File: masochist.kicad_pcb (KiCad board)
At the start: 2 copper layers, 77 parts, among them J1 USB_C_Receptacle_USB2.0, J2 AVR-ISP-6, SW1 RESET, SW2 SW_Push, U1 ATmega328P-PU, Y1 Crystal

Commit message: Project is NOT dead, components are roughly in place
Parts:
- moved Y1 225.3 mm to (232.3, 48.8)
- moved R5 222.6 mm to (201.9, 46.2)
- moved C1 222.1 mm to (227.3, 49.9), turned to 90 degrees
- moved C5 221.5 mm to (232.3, 34.2), turned to 180 degrees
- moved C2 211.0 mm to (242.1, 49.9), turned to 90 degrees
- moved R4 206.2 mm to (201.9, 43.4)
- moved R2 205.1 mm to (201.9, 40.6)
- moved R7 203.6 mm to (201.9, 51.8)
- moved R1 202.8 mm to (201.9, 35.1)
- moved R3 202.0 mm to (201.9, 37.8)
- moved R6 200.6 mm to (201.9, 49.0)
- moved DZ1 199.2 mm to (181.0, 51.8), turned to 180 degrees
- moved C4 198.4 mm to (220.0, 47.6)
- moved DZ2 197.3 mm to (181.0, 49.0), turned to 180 degrees
- moved SW2 162.2 mm to (129.2, 34.7)
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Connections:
- U1 pad 4: Net-(U1-Pad4) -> D+
- U1 pad 5: Net-(U1-Pad5) -> D-

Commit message: actually putting down some traces
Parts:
- moved D5 6.55 mm to (69.8, 44.5)
- moved D11 6.55 mm to (90.2, 44.5)
- moved D8 6.55 mm to (80.0, 44.5)
- moved D3 6.50 mm to (86.4, 43.1)
- moved D1 6.48 mm to (76.2, 43.2)
- moved D6 6.48 mm to (96.5, 43.2)
- moved D2 0.16 mm to (73.0, 43.8)
- moved D7 0.16 mm to (93.3, 43.8)
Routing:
- net Net-(D8-Pad2): track 0.00 -> 62.9 mm
- net Net-(D5-Pad2): track 0.00 -> 58.4 mm
- net Net-(D17-Pad2): track 0.00 -> 53.4 mm
- net Net-(D14-Pad2): track 0.00 -> 53.4 mm
- net Net-(D21-Pad2): track 0.00 -> 53.4 mm
- net Net-(D11-Pad2): track 0.00 -> 53.4 mm
- net Net-(D4-Pad2): track 0.00 -> 38.7 mm
- net Net-(D2-Pad2): track 0.00 -> 36.7 mm
- net Net-(D7-Pad2): track 0.00 -> 30.2 mm
- net Net-(D10-Pad2): track 0.00 -> 30.2 mm
- net Net-(D16-Pad2): track 0.00 -> 30.2 mm
- net Net-(D13-Pad2): track 0.00 -> 30.2 mm
- net Net-(D3-Pad2): track 0.00 -> 16.7 mm
- net Net-(D1-Pad2): track 0.00 -> 15.0 mm
- net Net-(D9-Pad2): track 0.00 -> 9.09 mm
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
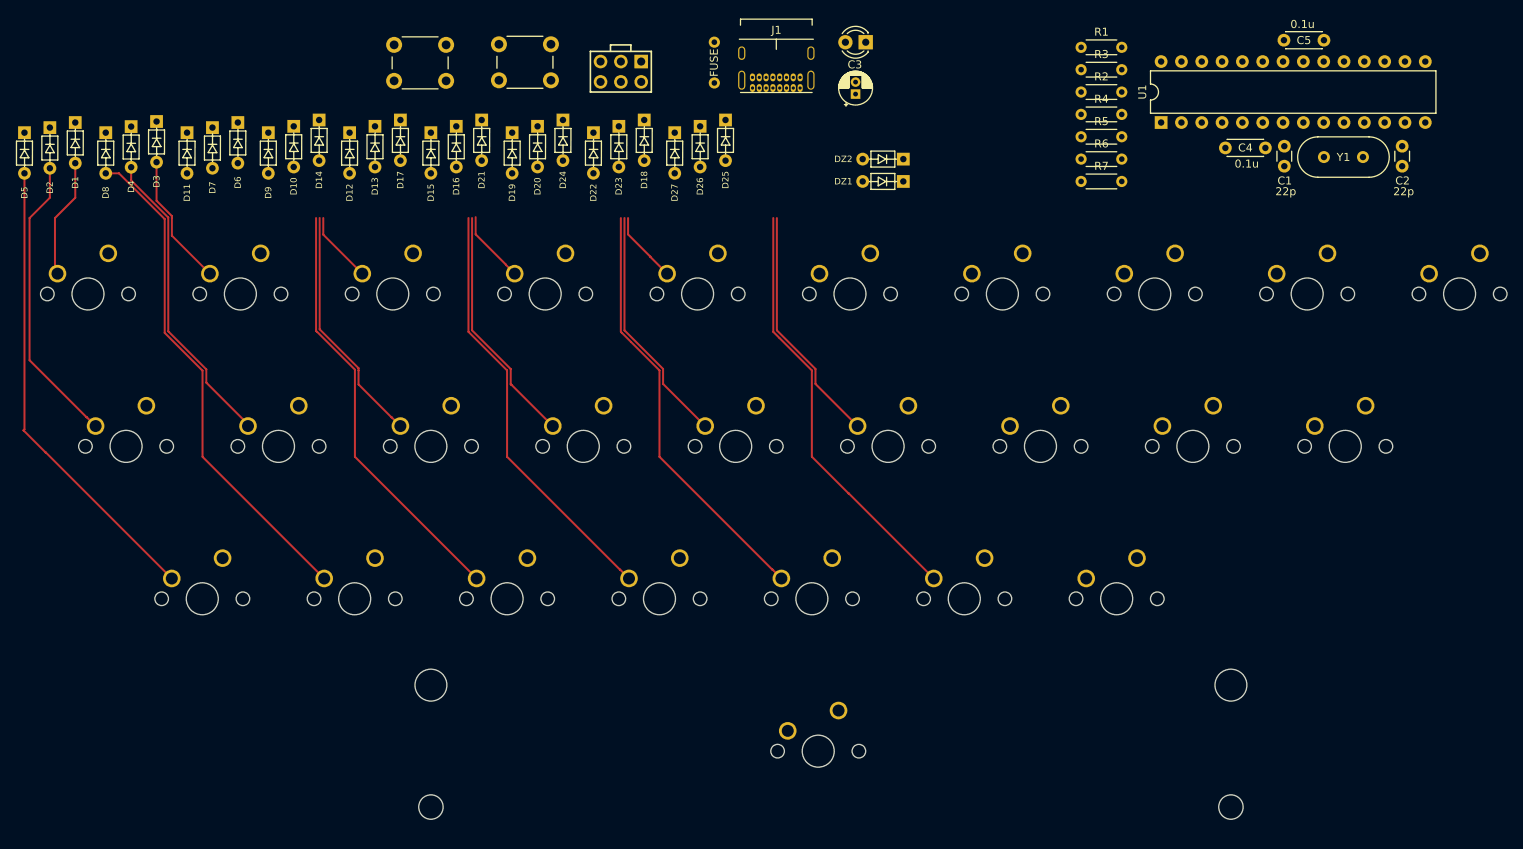
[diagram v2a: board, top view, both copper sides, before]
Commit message: More traces (switches and matrix diodes)
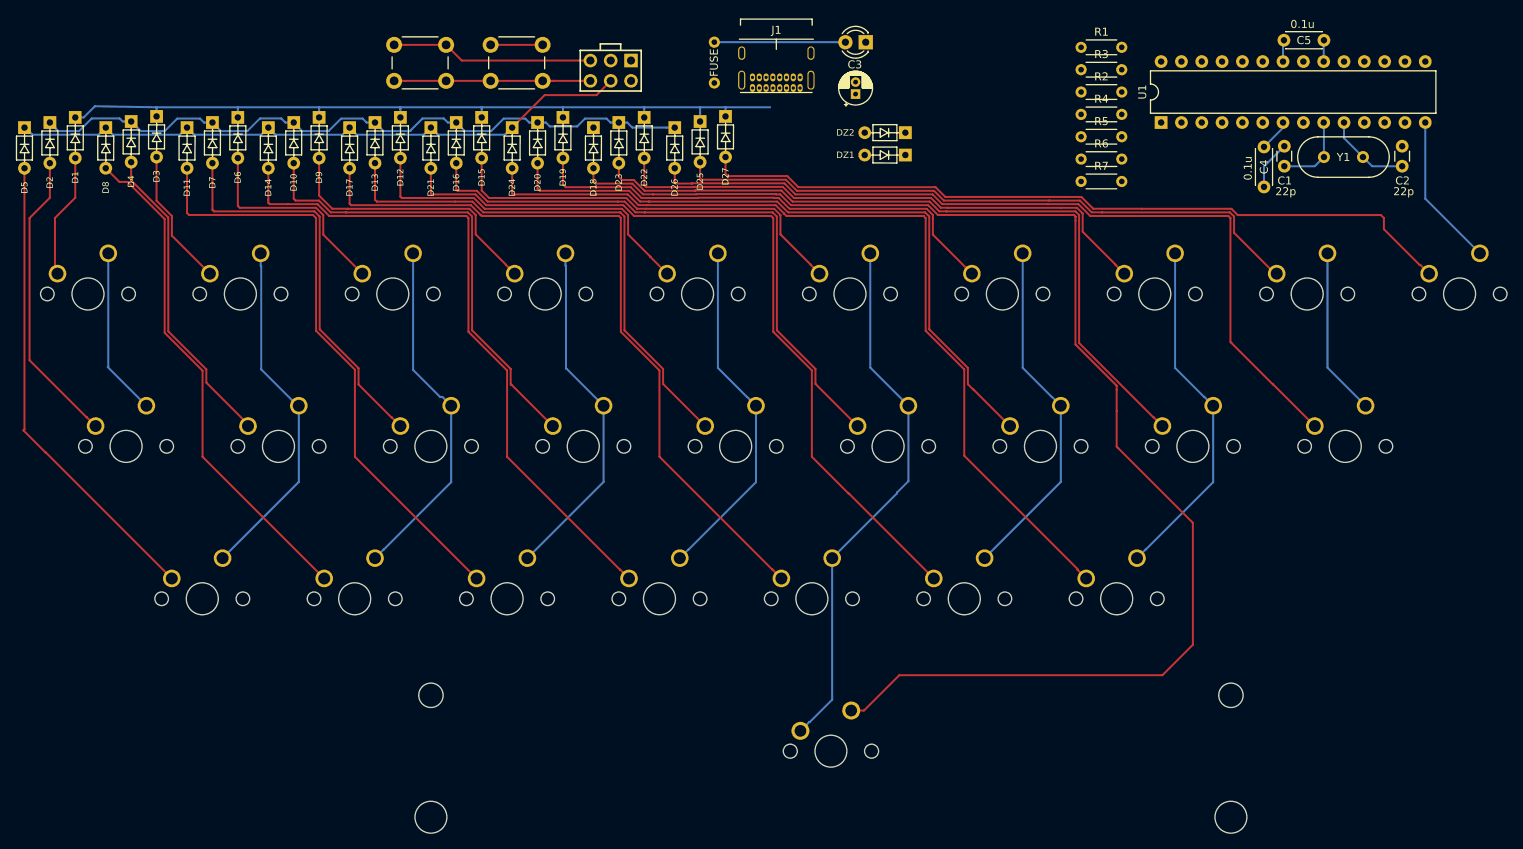
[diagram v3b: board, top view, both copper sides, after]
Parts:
- removed ST62: 6.25U, cftkb:MX-6.25U-Stabilizer
- KC_SPC1: footprint cftkb:SW_Cherry_MX1A_1.00u_PCB-NOSCREEN -> MX_Only:MXOnly-6.25U-NoLED
- moved SW2 7.12 mm to (134.6, 39.2), turned to 180 degrees
- moved D27 6.67 mm to (157.5, 42.4)
- moved D12 6.63 mm to (116.8, 42.5)
- moved D9 6.63 mm to (106.7, 42.5)
- moved D15 6.63 mm to (127.0, 42.5)
- moved D19 6.63 mm to (137.2, 42.5)
- moved D22 6.63 mm to (147.3, 42.5)
- moved D14 6.42 mm to (100.3, 43.8)
- moved D17 6.42 mm to (110.5, 43.8)
- moved D18 6.42 mm to (141.0, 43.8)
- moved D21 6.42 mm to (120.7, 43.8)
- moved D24 6.42 mm to (130.8, 43.8)
- moved KC_SPC1 5.17 mm to (170.7, 123.0)
- moved C4 4.83 mm to (224.8, 47.5), turned to 270 degrees
- moved DZ1 3.31 mm to (181.2, 48.5)
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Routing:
- net Net-(D18-Pad2): track 0.00 -> 169.6 mm
- net Net-(D24-Pad2): track 0.00 -> 108.9 mm
- net Net-(D26-Pad2): track 0.00 -> 103.6 mm
- net ROW0: track 0.00 -> 99.1 mm
- net Net-(D27-Pad2): track 0.00 -> 96.1 mm
- net Net-(D23-Pad2): track 0.00 -> 92.0 mm
- net ROW1: track 0.00 -> 87.3 mm
- net Net-(D20-Pad2): track 0.00 -> 83.3 mm
- net Net-(D25-Pad2): track 0.00 -> 80.2 mm
- net ROW2: track 0.00 -> 80.1 mm
- net Net-(D22-Pad2): track 0.00 -> 69.4 mm
- net COL5: track 0.00 -> 67.3 mm
- net Net-(D19-Pad2): track 0.00 -> 60.0 mm
- net Net-(D15-Pad2): track 0.00 -> 51.4 mm
- net Net-(D21-Pad2): track 53.4 -> 100.0 mm
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
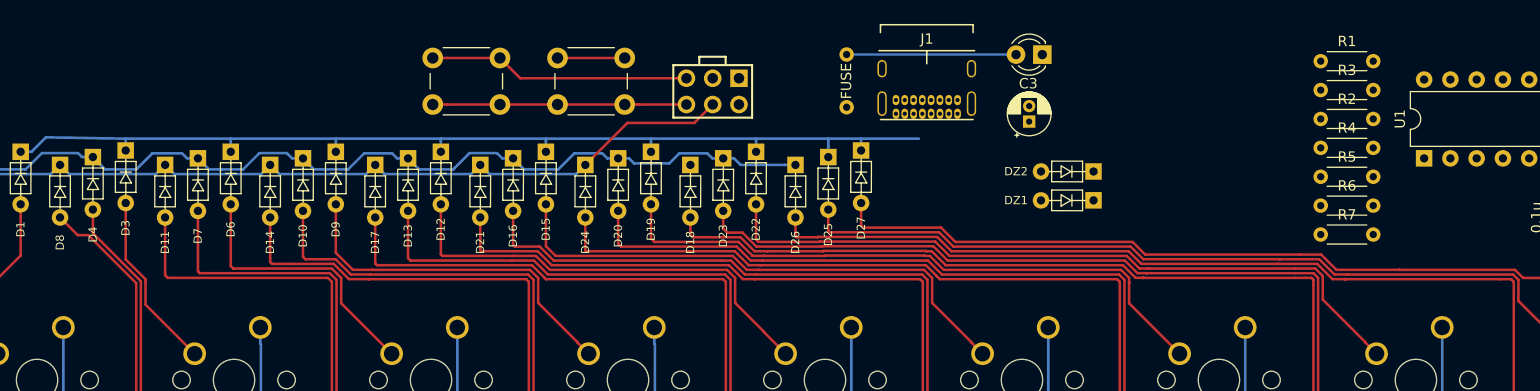
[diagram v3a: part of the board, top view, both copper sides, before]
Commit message: reassigning pins to hopefully make routing easier
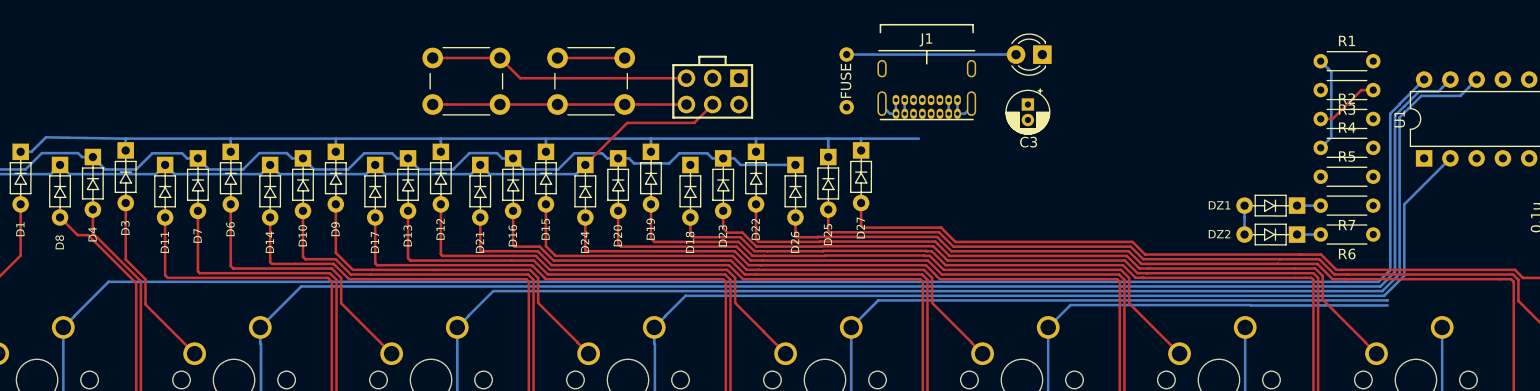
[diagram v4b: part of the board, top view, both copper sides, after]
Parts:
- moved DZ2 20.6 mm to (200.9, 51.8)
- moved DZ1 19.7 mm to (200.9, 49.0)
- moved R6 5.80 mm to (207.0, 51.8), turned to 180 degrees
- moved R7 5.80 mm to (207.0, 49.0), turned to 180 degrees
- moved R3 5.08 mm to (207.0, 37.8), turned to 180 degrees
- moved C3 1.66 mm to (173.6, 39.2), turned to 270 degrees
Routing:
- net COL0: track 21.1 -> 171.5 mm
- net COL1: track 44.1 -> 178.0 mm
- net COL2: track 44.2 -> 161.7 mm
- net COL3: track 44.0 -> 131.9 mm
- net COL4: track 44.1 -> 97.0 mm
- net COL5: track 67.3 -> 101.0 mm
- net GND: track 33.5 -> 49.0 mm
- net +5V: track 23.1 -> 32.3 mm
- net Net-(F1-Pad2): track 0.00 -> 2.65 mm
- net Net-(DZ2-Pad1): track 0.00 -> 2.29 mm
- net Net-(DZ1-Pad1): track 0.00 -> 2.29 mm

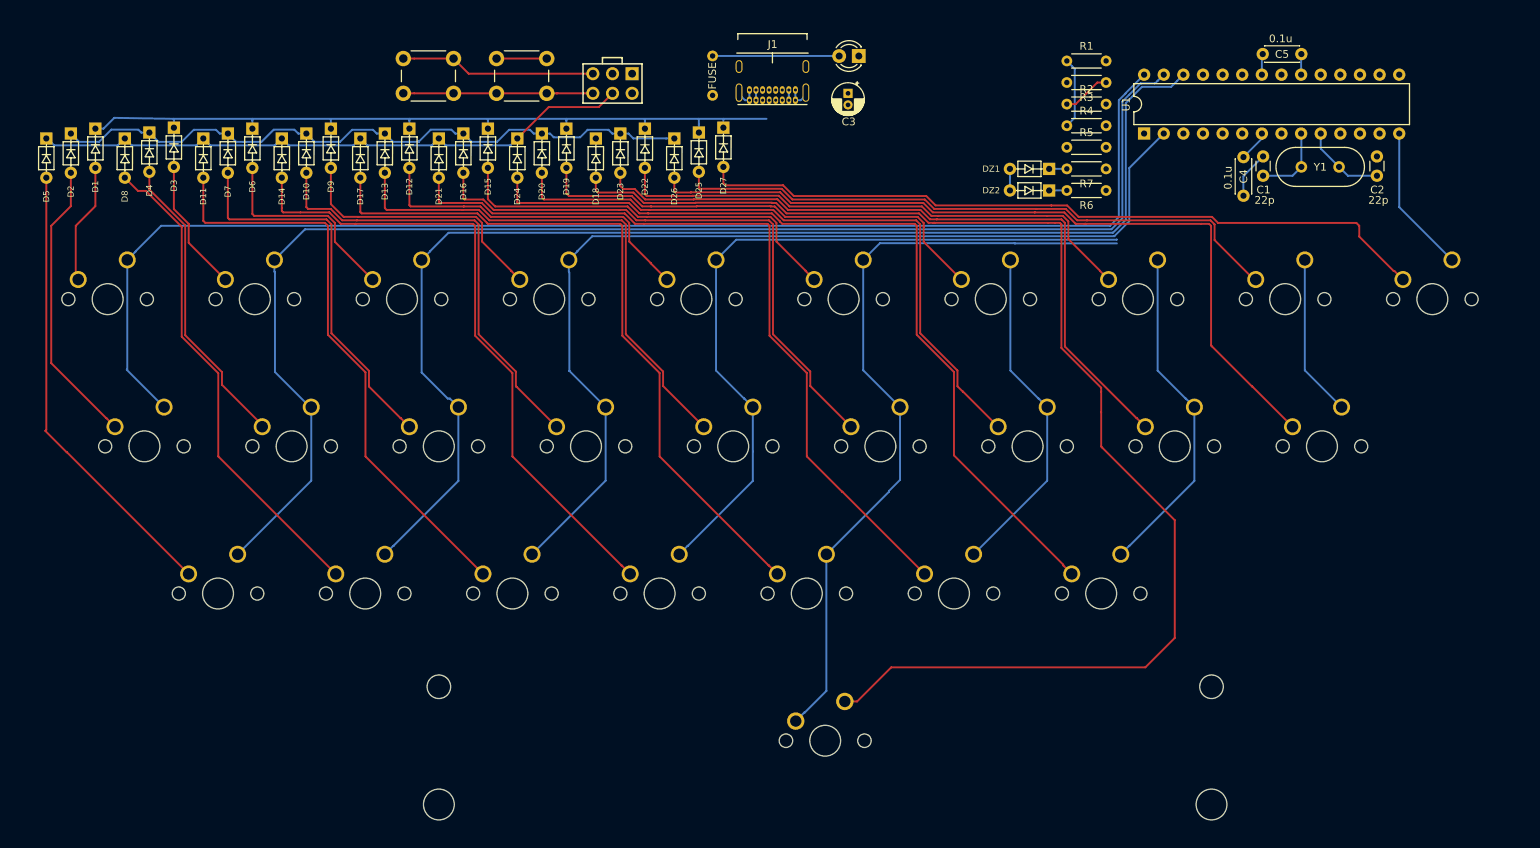
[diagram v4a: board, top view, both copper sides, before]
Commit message: added PCB edges so I could see the render
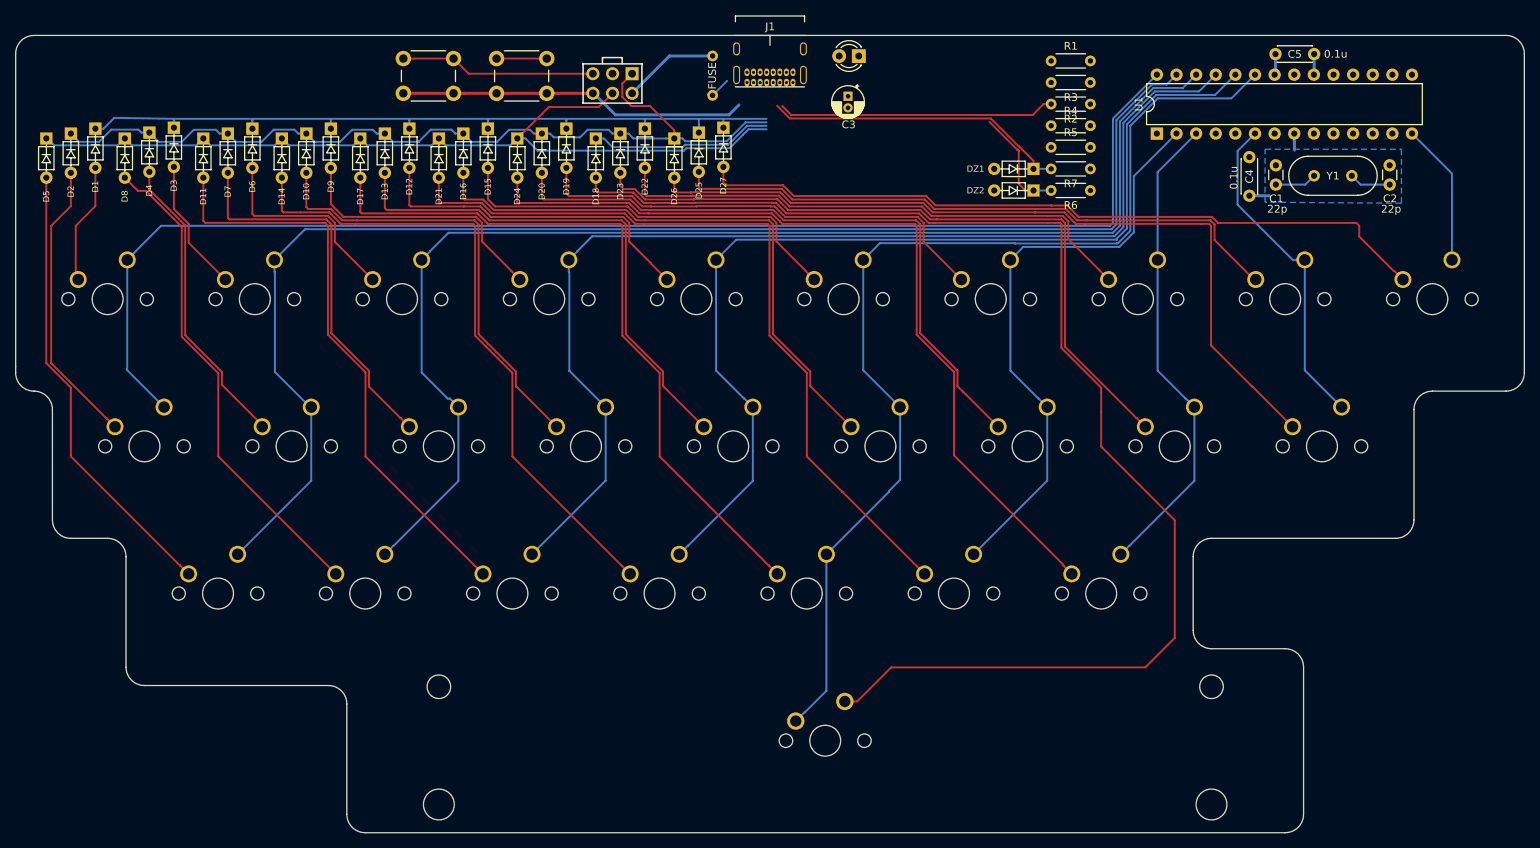
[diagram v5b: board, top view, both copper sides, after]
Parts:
- moved R2 3.05 mm to (205.0, 40.6), turned to 180 degrees
- moved J1 2.31 mm to (163.5, 31.8)
- moved R1 2.03 mm to (199.9, 35.1)
- moved R4 2.03 mm to (199.9, 43.4)
- moved R5 2.03 mm to (199.9, 46.2)
- moved DZ1 2.03 mm to (198.9, 49.0)
- moved DZ2 2.03 mm to (198.9, 51.8)
- moved R3 2.03 mm to (205.0, 37.8)
- moved R6 2.03 mm to (205.0, 51.8)
- moved R7 2.03 mm to (205.0, 49.0)
- moved Y1 2.01 mm to (233.9, 49.9)
- moved C1 2.01 mm to (229.0, 51.1)
- moved C2 2.01 mm to (243.7, 51.1)
- moved C5 1.65 mm to (233.9, 34.2)
- moved U1 1.65 mm to (213.6, 44.5)
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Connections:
- U1 pad 2: COL3 -> COL6
- U1 pad 23: COL7 -> COL5
- U1 pad 24: COL6 -> COL4
- U1 pad 25: COL4 -> COL3
- U1 pad 3: COL5 -> COL7
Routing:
- net Net-(DZ1-Pad1): track 2.29 -> 39.4 mm
- net Net-(J1-PadA5): track 0.00 -> 35.9 mm
- net COL5: track 101.0 -> 135.9 mm
- net ROW2: track 80.1 -> 114.2 mm
- net COL6: track 44.0 -> 76.6 mm
- net COL4: track 97.0 -> 129.2 mm
- net ROW1: track 87.3 -> 113.5 mm
- net ROW3: track 0.00 -> 23.7 mm
- net COL8: track 21.0 -> 42.8 mm
- net COL7: track 44.1 -> 62.5 mm
- net +5V: track 32.3 -> 16.0 mm
- net COL3: track 131.9 -> 145.6 mm
- net Net-(DZ2-Pad1): track 2.29 -> 14.1 mm
- net XTAL2: track 10.7 -> 5.37 mm
- net GND: track 49.0 -> 53.4 mm
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- added copper zone on B.Cu, net GND
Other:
- board outline added: 195.3 x 103.2 mm
- net class Power added: clearance 0.2, trace_width 0.38, via_dia 0.8, via_drill 0.4
